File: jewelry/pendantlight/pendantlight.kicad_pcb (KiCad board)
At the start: 2 copper layers, 5 x 40 mm, 7 parts, among them J1 Conn_01x01, J2 Conn_01x01, J3 Conn_01x01, J4 Conn_01x01

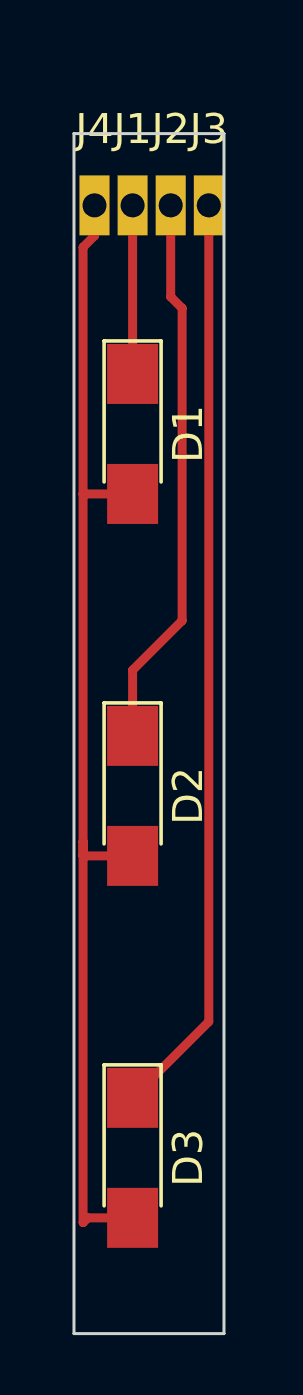
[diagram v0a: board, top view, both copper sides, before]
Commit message: jewelry: Include current limiting resistors
Can then be plug&play with 3.3V+ sources
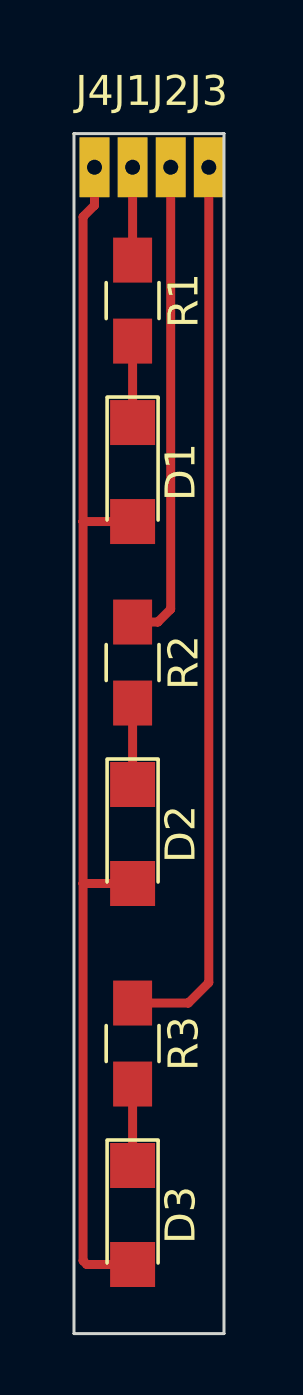
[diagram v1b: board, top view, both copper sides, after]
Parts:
- added R1: 47R, Resistors_SMD:R_0805_HandSoldering, F.Cu at (148.0, 115.6)
- added R2: 47R, Resistors_SMD:R_0805_HandSoldering, F.Cu at (148.0, 127.6)
- added R3: 47R, Resistors_SMD:R_0805_HandSoldering, F.Cu at (148.0, 140.3)
- D1, D2, D3: footprint LEDs:LED_1206_HandSoldering -> LEDs:LED_1206
- moved D3 1.91 mm to (148.0, 146.1)
- moved D1 1.27 mm to (148.0, 121.3)
- moved J1 1.27 mm to (148.0, 111.1)
- moved J2 1.27 mm to (149.2, 111.1)
- moved J3 1.27 mm to (150.5, 111.1)
- moved J4 1.27 mm to (146.7, 111.1)
- moved D2 1.27 mm to (148.0, 133.3)
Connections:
- J1 pad 1: Net-(D1-Pad1) -> Net-(J1-Pad1)
- J2 pad 1: Net-(D2-Pad1) -> Net-(J2-Pad1)
- J3 pad 1: Net-(D3-Pad1) -> Net-(J3-Pad1)
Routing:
- net Net-(J3-Pad1): track 0.00 -> 30.0 mm
- net Net-(D3-Pad1): track 30.8 -> 2.72 mm
- net Net-(J2-Pad1): track 0.00 -> 16.2 mm
- net Net-(D2-Pad1): track 18.5 -> 2.71 mm
- net Net-(J1-Pad1): track 0.00 -> 3.09 mm
- net Net-(D1-Pad1): track 5.62 -> 2.72 mm
- net Net-(D1-Pad2): track 39.6 -> 41.6 mm
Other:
- net class Default: clearance 0.3 -> 0.24
- rule trace_clearance: 0.3 -> 0.24
